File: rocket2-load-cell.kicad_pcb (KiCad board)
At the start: 2 copper layers, 45 x 90 mm, 47 parts, among them J1 SWD, J3 PJ-002A, J4 Conn_01x02, J5 USB_C_Receptacle_USB2.0_14P, U1 STM32F103C8Tx, U3 LD1117V33, Y1 16MHz

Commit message: Revisions from review. DO NOT USE. please use this as reference since the traces aren't ideal. There are 2 violations (silkscreen clipping) which can easily be fixed and no errors. if you have any more, something is wrong.
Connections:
- GX-16 pad 2: GND -> VLC
- GX-16 pad 3: VLC -> GND
- J5 pad A6: unconnected-(J5-D+-PadA6) -> USB_D+
- J5 pad A7: unconnected-(J5-D--PadA7) -> USB_D-
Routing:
- net +3.3V: track 172.2 -> 200.3 mm
- net VLC: track 13.1 -> 20.5 mm
- net USB_VBUS: track 4.59 -> 7.76 mm, vias 0 -> 2
- net GND: track 38.2 -> 35.5 mm, vias 88 -> 89
- net USB_D+: track 16.1 -> 18.5 mm
- net USB_D-: track 16.2 -> 18.1 mm

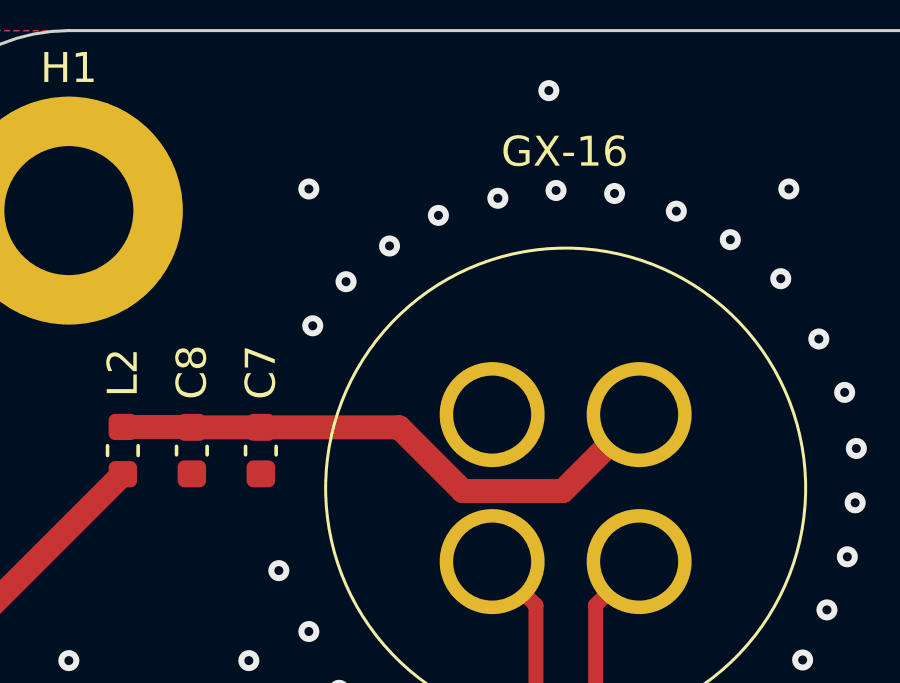
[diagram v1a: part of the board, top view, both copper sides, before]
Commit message: Revised GX port rec
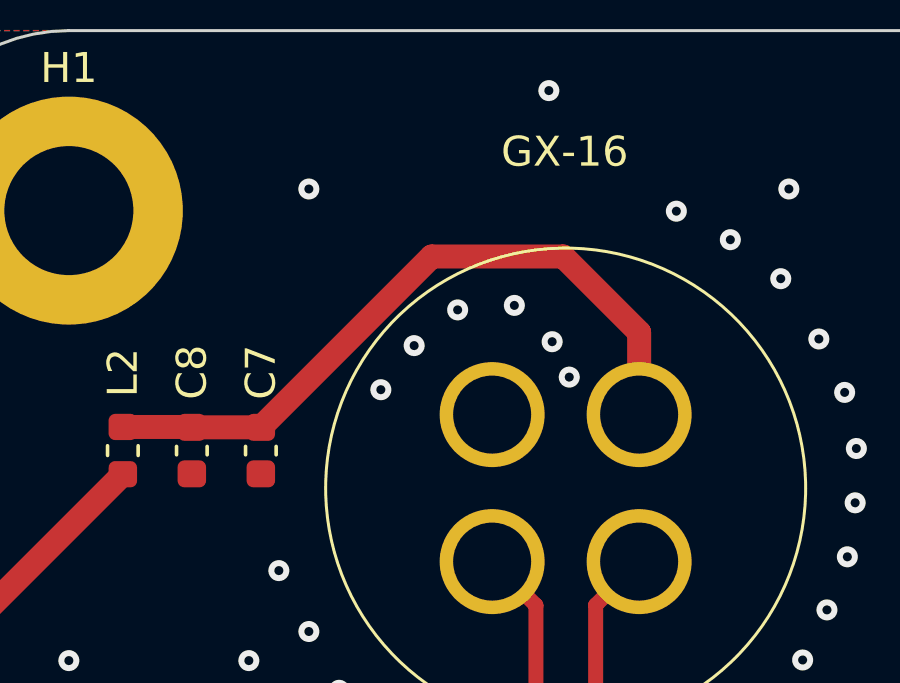
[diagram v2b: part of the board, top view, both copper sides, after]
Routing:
- net VLC: track 20.5 -> 24.7 mm
- net GND: vias 89 -> 88
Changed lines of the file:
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@@
 	)
 	(via
-		(at 125.24 58.36976)
+		(at 127.51 60.5)
 		(size 0.7)
 		(drill 0.3)
@@
 	)
 	(via
-		(at 134.19 55.42976)
-		(size 0.7)
-		(drill 0.3)
-		(layers "F.Cu" "B.Cu")
-		(free yes)
-		(net 2)
-	)
-	(via
-		(at 130.3 55.58976)
-		(size 0.7)
-		(drill 0.3)
-		(layers "F.Cu" "B.Cu")
-		(free yes)
-		(net 2)
-	)
-	(via
 		(at 125.5 99.9)
 		(size 0.7)
@@
 	)
 	(via
-		(at 128.32 56.15976)
+		(at 130.85 59.16)
 		(size 0.7)
 		(drill 0.3)
@@
 	)
 	(via
-		(at 124.13 59.83976)
+		(at 126.4 61.97)
 		(size 0.7)
 		(drill 0.3)
@@
 	)
 	(via
+		(at 132.11 60.37)
+		(size 0.7)
+		(drill 0.3)
+		(layers "F.Cu" "B.Cu")
+		(free yes)
+		(net 2)
+	)
+	(via
 		(at 124 55.27976)
 		(size 0.7)
@@
 	)
 	(via
+		(at 132.68 61.55)
+		(size 0.7)
+		(drill 0.3)
+		(layers "F.Cu" "B.Cu")
+		(free yes)
+		(net 2)
+	)
+	(via
 		(at 126.31 73.2)
 		(size 0.7)
@@
 	)
 	(via
-		(at 132.24 55.33)
-		(size 0.7)
-		(drill 0.3)
-		(layers "F.Cu" "B.Cu")
-		(free yes)
-		(net 2)
-	)
-	(via
 		(at 123 68)
 		(size 0.7)
@@
 	)
 	(via
-		(at 126.69 57.17976)
+		(at 128.96 59.31)
 		(size 0.7)
 		(drill 0.3)
@@
 	)
 	(segment
-		(start 127.012183 63.225)
-		(end 129.136183 65.349)
+		(start 128.095 57.53)
+		(end 132.48 57.53)
 		(width 0.8)
 		(layer "F.Cu")
@@
 	)
 	(segment
-		(start 132.461 65.349)
-		(end 135.01 62.8)
+		(start 122.4 63.225)
+		(end 128.095 57.53)
 		(width 0.8)
 		(layer "F.Cu")
@@
 	)
 	(segment
+		(start 132.48 57.53)
+		(end 135.01 60.06)
+		(width 0.8)
+		(layer "F.Cu")
+		(net 5)
+	)
+	(segment
 		(start 120.1 63.225)
 		(end 122.4 63.225)
@@
 	)
 	(segment
-		(start 122.4 63.225)
-		(end 127.012183 63.225)
-		(width 0.8)
-		(layer "F.Cu")
-		(net 5)
-	)
-	(segment
-		(start 129.136183 65.349)
-		(end 132.461 65.349)
-		(width 0.8)
-		(layer "F.Cu")
+		(start 135.01 60.06)
+		(end 135.01 62.8)
+		(width 0.8)
+		(layer "F.Cu")

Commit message: cleaned up more with david (w message)
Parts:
- moved C4 0.20 mm to (142.4, 94.6)
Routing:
- net +3.3V: track 200.3 -> 217.0 mm, vias 4 -> 3
- net DEBUG_SWDIO: track 14.3 -> 18.9 mm
- net NRST: track 23.1 -> 23.8 mm, vias 0 -> 2
- net GND: vias 88 -> 90
